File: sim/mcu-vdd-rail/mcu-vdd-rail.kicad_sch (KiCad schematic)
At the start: 152 parts

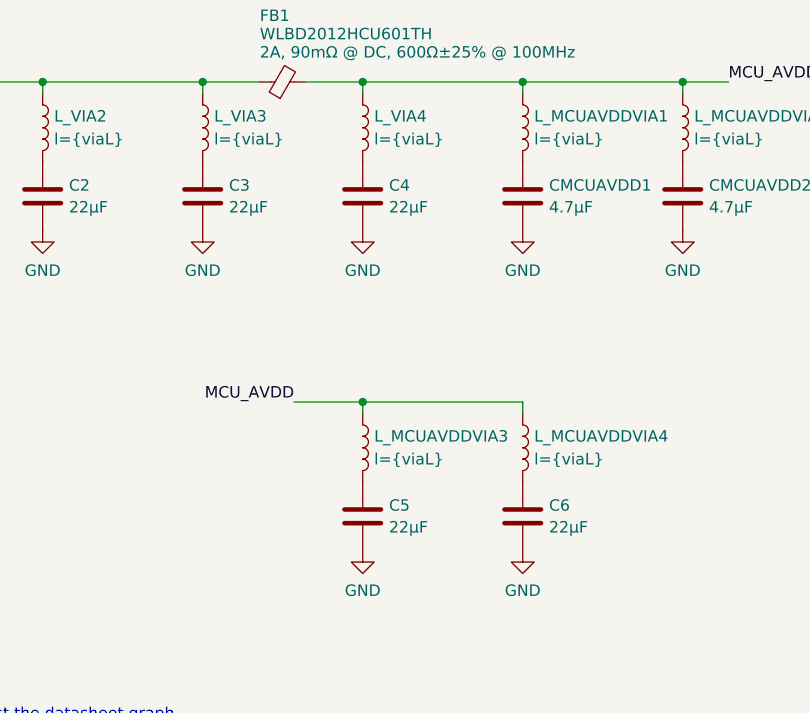
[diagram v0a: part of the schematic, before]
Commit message: Various tidy-ups and checks, mainly around the bypass capacitors.  Added a load of test points.
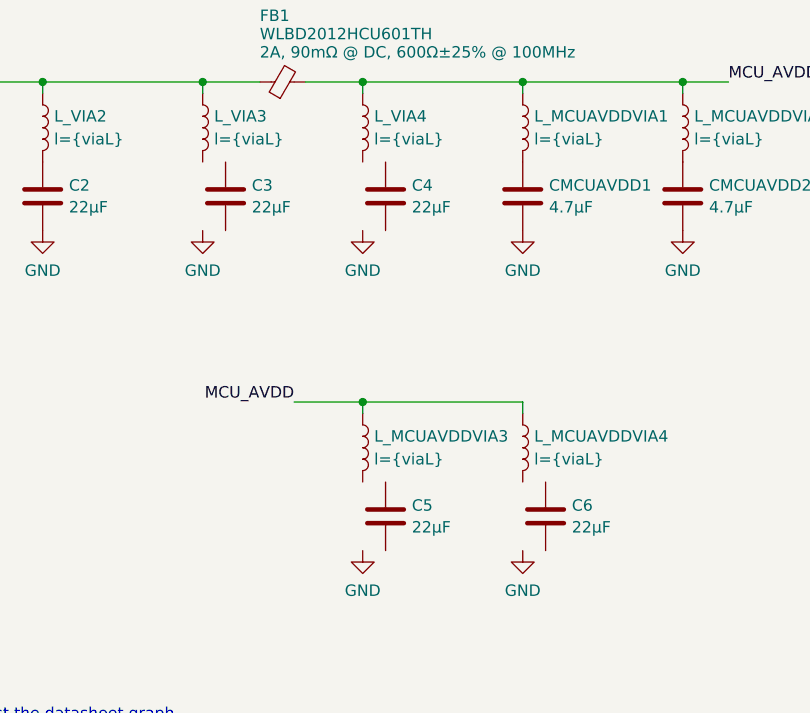
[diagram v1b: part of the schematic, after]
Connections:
- net 0: no longer C3.2, C4.2, C5.2, C6.2
- net at L_MCUAVDDVIA4.2 (P2): no longer C6.1
- net at C4.1: no longer L_VIA4.2 (P2)
- net at C3.1: no longer L_VIA3.2 (P2)
- net at L_MCUAVDDVIA3.2 (P2): no longer C5.1
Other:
- moved on the sheet: C3, C4, C5, C6
